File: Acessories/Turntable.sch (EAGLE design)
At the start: 34 parts, among them IC1 7812TV, IC2 7805TV, M1 ARDUINO-NANO-3.0, U2 A4988, X1 MKDSN1,5/4-5,08, X2 1751248, X3 1751264

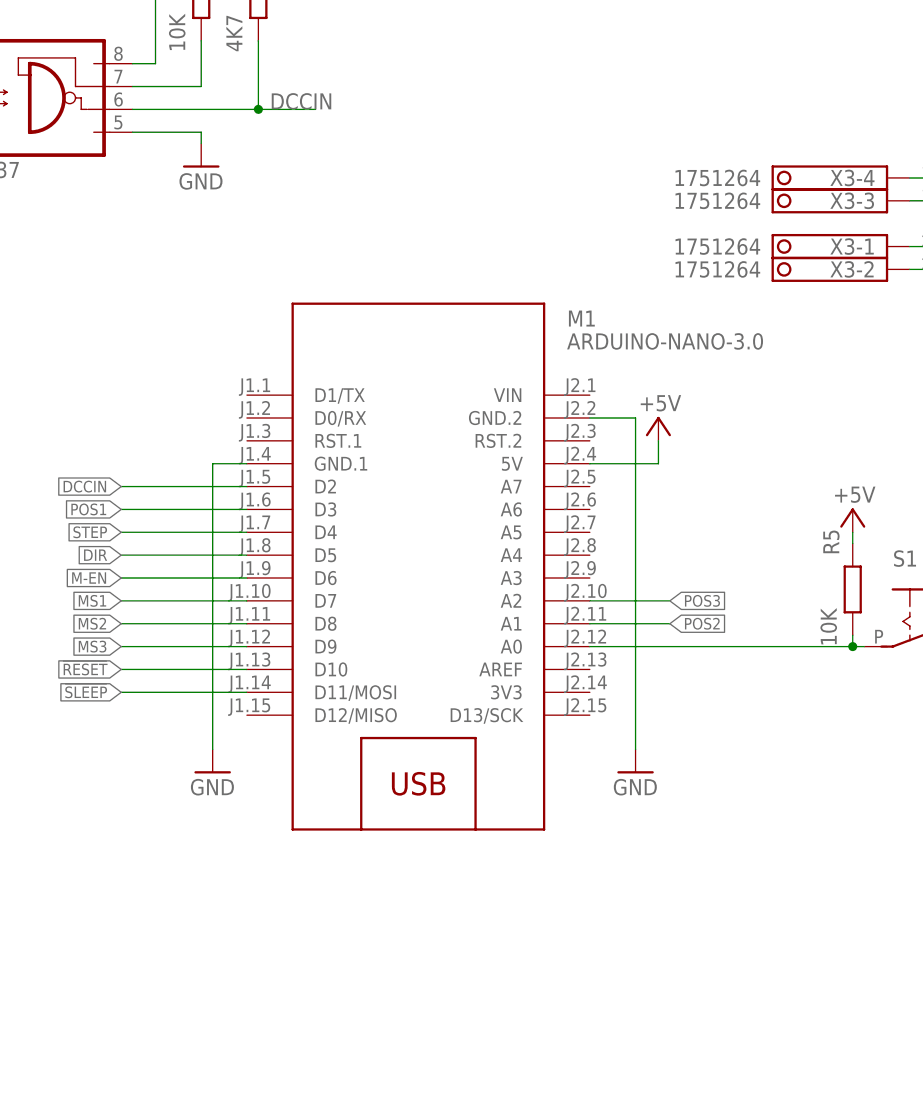
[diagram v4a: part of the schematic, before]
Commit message: Added connector for external stepper drive
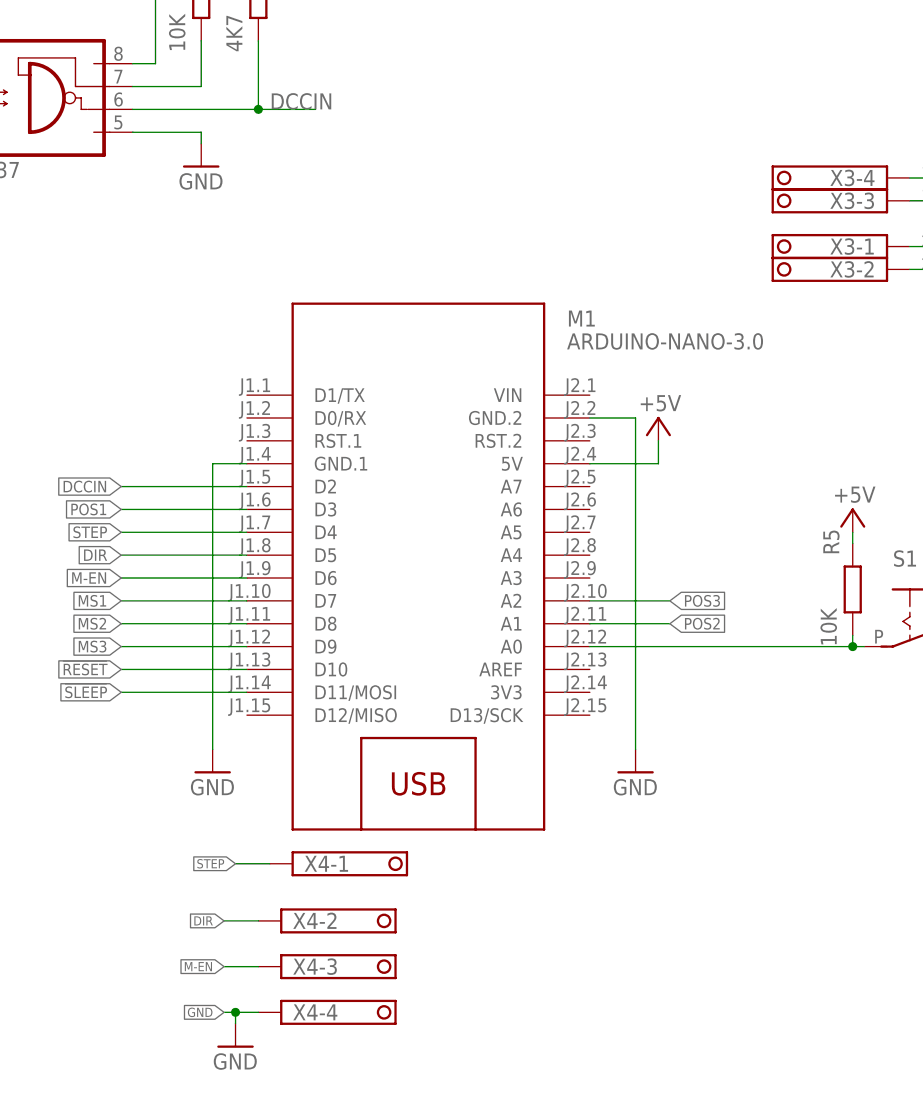
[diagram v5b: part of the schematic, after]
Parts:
- added X4: 1751264, con-phoenix-350:1751264
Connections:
- net DIR: now also X4-2.K
- net GND: now also X4-4.K
- net M-EN: now also X4-3.K
- net STEP: now also X4-1.K
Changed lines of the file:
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@@
 <?xml version="1.0" encoding="utf-8"?>
 <!DOCTYPE eagle SYSTEM "eagle.dtd">
-<eagle version="9.4.2">
+<eagle version="9.6.0">
 <drawing>
 <settings>
@@
 <part name="GND12" library="supply1" deviceset="GND" device=""/>
 <part name="JP4" library="adafruit" library_urn="urn:adsk.eagle:library:420" deviceset="PINHD-1X3" device="" package3d_urn="urn:adsk.eagle:package:6240710/1"/>
+<part name="X4" library="con-phoenix-350" deviceset="1751264" device=""/>
+<part name="GND1" library="supply1" deviceset="GND" device=""/>
 </parts>
 <sheets>
@@
 <instance part="X3" gate="-1" x="138.43" y="95.25" smashed="yes" rot="R180">
 <attribute name="NAME" x="137.16" y="96.139" size="1.778" layer="95" rot="R180"/>
-<attribute name="VALUE" x="124.46" y="96.139" size="1.778" layer="96" rot="R180"/>
 </instance>
 <instance part="X3" gate="-3" x="138.43" y="100.33" smashed="yes" rot="R180">
 <attribute name="NAME" x="137.16" y="101.219" size="1.778" layer="95" rot="R180"/>
-<attribute name="VALUE" x="124.46" y="101.219" size="1.778" layer="96" rot="R180"/>
 </instance>
 <instance part="X3" gate="-4" x="138.43" y="102.87" smashed="yes" rot="R180">
 <attribute name="NAME" x="137.16" y="103.759" size="1.778" layer="95" rot="R180"/>
-<attribute name="VALUE" x="124.46" y="103.759" size="1.778" layer="96" rot="R180"/>
 </instance>
 <instance part="X3" gate="-2" x="138.43" y="92.71" smashed="yes" rot="R180">
 <attribute name="NAME" x="137.16" y="93.599" size="1.778" layer="95" rot="R180"/>
-<attribute name="VALUE" x="124.46" y="93.599" size="1.778" layer="96" rot="R180"/>
 </instance>
 <instance part="JP3" gate="A" x="11.43" y="34.29" smashed="yes" rot="MR0">
@@
 <attribute name="NAME" x="17.78" y="19.685" size="1.778" layer="95" rot="MR0"/>
 <attribute name="VALUE" x="17.78" y="6.35" size="1.778" layer="96" rot="MR0"/>
+</instance>
+<instance part="X4" gate="-1" x="72.39" y="26.67" smashed="yes">
+<attribute name="NAME" x="73.66" y="25.781" size="1.778" layer="95"/>
+</instance>
+<instance part="X4" gate="-2" x="71.12" y="20.32" smashed="yes">
+<attribute name="NAME" x="72.39" y="19.431" size="1.778" layer="95" font="vector"/>
+</instance>
+<instance part="X4" gate="-3" x="71.12" y="15.24" smashed="yes">
+<attribute name="NAME" x="72.39" y="14.351" size="1.778" layer="95" font="vector"/>
+</instance>
+<instance part="X4" gate="-4" x="71.12" y="10.16" smashed="yes">
+<attribute name="NAME" x="72.39" y="9.271" size="1.778" layer="95" font="vector"/>
+</instance>
+<instance part="GND1" gate="1" x="66.04" y="6.35" smashed="yes">
+<attribute name="VALUE" x="63.5" y="3.81" size="1.778" layer="96"/>
 </instance>
 </instances>
@@
 <junction x="20.32" y="11.43"/>
 </segment>
+<segment>
+<pinref part="X4" gate="-4" pin="K"/>
+<wire x1="68.58" y1="10.16" x2="66.04" y2="10.16" width="0.1524" layer="91"/>
+<label x="64.77" y="10.16" size="1.016" layer="95" rot="R180" xref="yes"/>
+<pinref part="GND1" gate="1" pin="GND"/>
+<wire x1="66.04" y1="10.16" x2="64.77" y2="10.16" width="0.1524" layer="91"/>
+<wire x1="66.04" y1="8.89" x2="66.04" y2="10.16" width="0.1524" layer="91"/>
+<junction x="66.04" y="10.16"/>
+</segment>
 </net>
 <net name="+5V" class="0">
@@
 <label x="194.31" y="85.09" size="1.27" layer="95" xref="yes"/>
 </segment>
+<segment>
+<pinref part="X4" gate="-3" pin="K"/>
+<wire x1="68.58" y1="15.24" x2="64.77" y2="15.24" width="0.1524" layer="91"/>
+<label x="64.77" y="15.24" size="1.016" layer="95" rot="R180" xref="yes"/>
+</segment>
 </net>
 <net name="POS1" class="0">
@@
 <label x="193.04" y="105.41" size="1.27" layer="95" xref="yes"/>
 </segment>
+<segment>
+<pinref part="X4" gate="-1" pin="K"/>
+<wire x1="69.85" y1="26.67" x2="66.04" y2="26.67" width="0.1524" layer="91"/>
+<label x="66.04" y="26.67" size="1.016" layer="95" rot="R180" xref="yes"/>
+</segment>
 </net>
 <net name="DIR" class="0">
@@
 <label x="53.34" y="60.96" size="1.27" layer="95" rot="R180" xref="yes"/>
 </segment>
-</net>
+<segment>
+<pinref part="X4" gate="-2" pin="K"/>
+<wire x1="68.58" y1="20.32" x2="64.77" y2="20.32" width="0.1524" layer="91"/>
+<label x="64.77" y="20.32" size="1.016" layer="95" rot="R180" xref="yes"/>
+</segment>
+</net>
